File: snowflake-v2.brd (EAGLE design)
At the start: 68.6 x 68.6 mm, 32 parts, among them J1 M03X2-NOSILK, J2 CON_TERMINAL_HOLES, U2 V_REG_MCP170X-CB

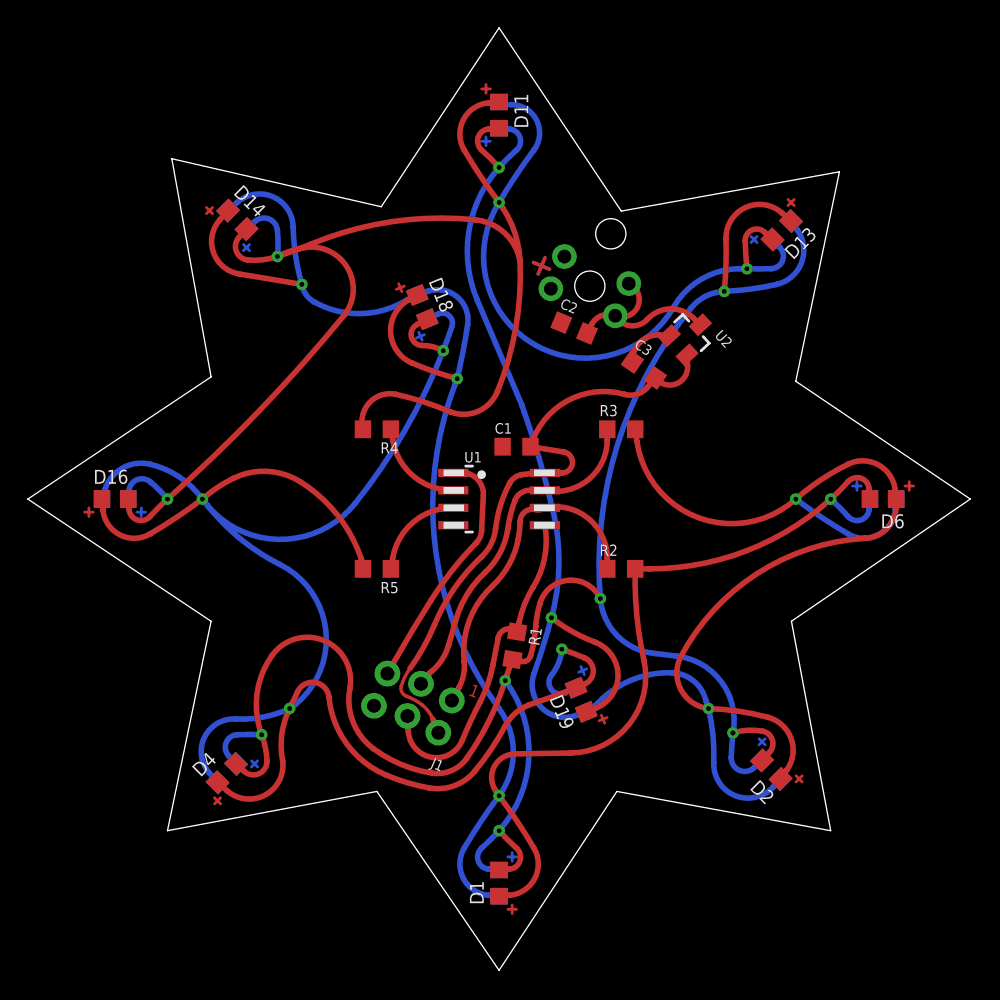
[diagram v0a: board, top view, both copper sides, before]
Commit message: Ground floods, vias, slights adjustmens to facilitate better flooding.
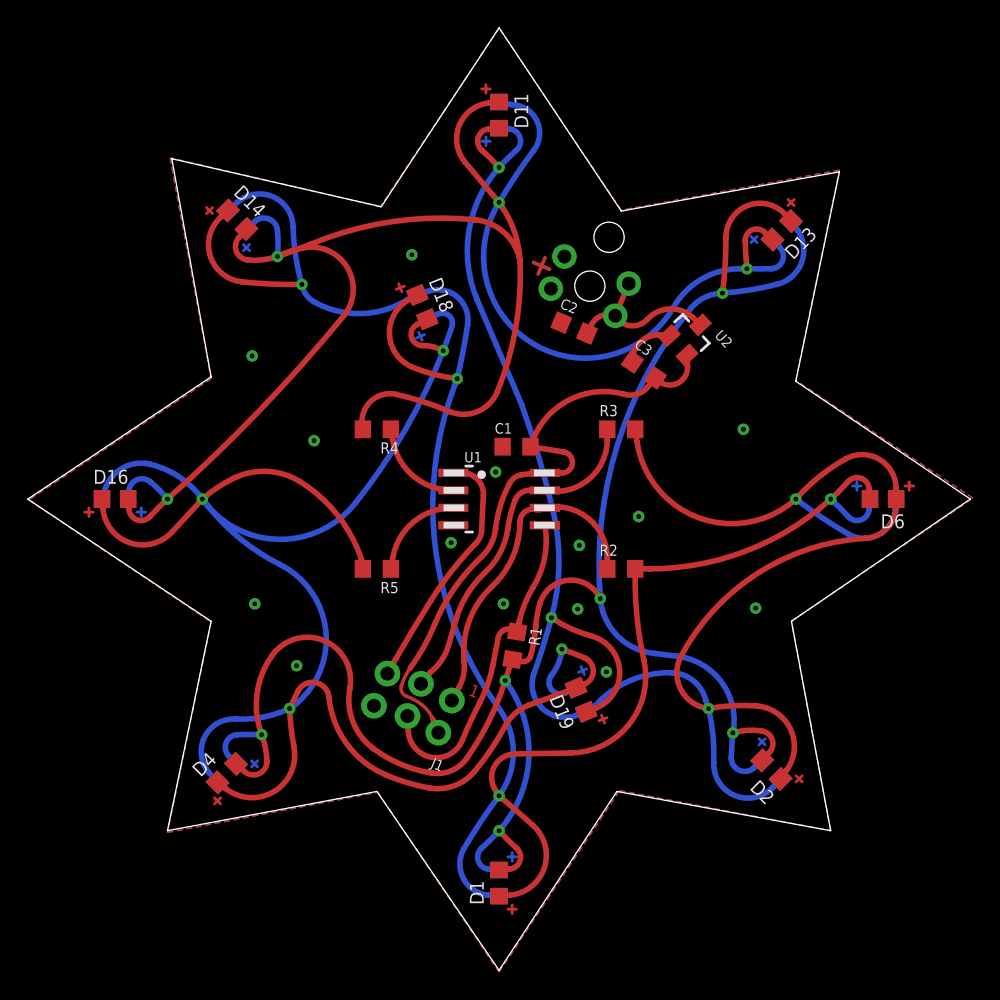
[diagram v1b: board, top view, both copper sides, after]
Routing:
- net N$7: track 145.7 -> 146.5 mm
- net N$10: track 135.5 -> 136.3 mm
- net N$8: track 141.2 -> 141.9 mm
- net GND: vias 0 -> 14
- added copper zone on layer 1, net GND
- added copper zone on layer 16, net GND
